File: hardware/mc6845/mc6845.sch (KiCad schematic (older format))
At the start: 20 parts, among them U1 MC6845, U10 AT28C16

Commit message: Add README, work on bitmap mode
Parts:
- J1: renamed from J?; footprint (none) -> Connector_PinHeader_2.54mm:PinHeader_2x20_P2.54mm_Vertical
- U10: footprint (none) -> Package_DIP:DIP-24_W10.16mm_Socket_LongPads
- U11, U13, U14, U15: renamed from U?; footprint (none) -> Package_DIP:DIP-14_W7.62mm_Socket_LongPads
- U12, U16, U17: renamed from U?; footprint (none) -> Package_DIP:DIP-16_W7.62mm_Socket_LongPads
- U2, U7: renamed from U?; footprint (none) -> Package_DIP:DIP-20_W7.62mm_Socket_LongPads
- X1: renamed from X?; footprint Oscillator:Oscillator_DIP-14 -> Package_DIP:DIP-4_W7.62mm_Socket_LongPads
- gave numbers to parts that had none: 1

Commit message: working on memory
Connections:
- net labels added: A[15..0], MA[15..0], PAGE[2..0]
- net labels removed: A[13..0], MA12, MA13, MA[13..0]
- wire segments 231 -> 229
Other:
- note added: "MA[15..12] to mux (RA, latch)"
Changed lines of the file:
@@
 F0 "memory" 50
 F1 "memory.sch" 50
-F2 "MA[13..0]" I L 6075 1300 50
-F3 "A[13..0]" I L 6075 1450 50
+F2 "MA[15..0]" I L 6075 1300 50
+F3 "A[15..0]" I L 6075 1450 50
 F4 "D[7..0]" B R 7075 1300 50
 F5 "LD[7..0]" O R 7075 1450 50
@@
 F10 "nBE" I L 6075 2225 50
 F11 "CCLK" I L 6075 2350 50
+F12 "MA[15..0]" I L 6075 2500 50
 $EndSheet
 Wire Bus Line
@@
 	7075 1300 7450 1300
 Text Label 5975 1300 2    50   ~ 0
-MA[13..0]
+MA[15..0]
 Wire Bus Line
 	7075 1450 7450 1450
@@
 D[7..0]
 Text Label 5675 1450 0    50   ~ 0
-A[13..0]
+A[15..0]
 Wire Wire Line
 	8000 2100 7650 2100
@@
 Wire Wire Line
 	4775 2475 5200 2475
-Text Label 5100 2275 2    50   ~ 0
-MA13
-Wire Wire Line
-	4775 2275 5200 2275
-Text Label 5100 2175 2    50   ~ 0
-MA12
-Wire Wire Line
-	4775 2175 5200 2175
 Text Label 5100 2075 2    50   ~ 0
 MA11
@@
 Wire Wire Line
 	8100 3875 8100 4325
+Wire Bus Line
+	6075 2500 5650 2500
+Text Label 5650 2500 0    50   ~ 0
+PAGE[2..0]
+Text Notes 5425 2975 0    75   ~ 0
+MA[15..12] to mux (RA, latch)
 $EndSCHEMATC

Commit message: working on 3D
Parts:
- removed A1: Arduino_UNO_R3, Module:Arduino_UNO_R3, symbol MCU_Module:Arduino_UNO_R3
- removed U2, U7: 74LS374, Package_DIP:DIP-20_W7.62mm_Socket_LongPads, symbol 74xx:74LS374
- removed X1: 25.175_DIP14, Package_DIP:DIP-4_W7.62mm_Socket_LongPads, symbol Oscillator:CXO_DIP14
- added X1: 25.175MHz, Package_DIP:DIP-8_W7.62mm_LongPads, symbol Oscillator:SG-8002DC
- U10: footprint Package_DIP:DIP-24_W10.16mm_Socket_LongPads -> Package_DIP:DIP-24_W15.24mm_LongPads
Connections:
- wire segments 229 -> 172
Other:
- note removed: "ADDRESS LATCH\n(Arduino)"

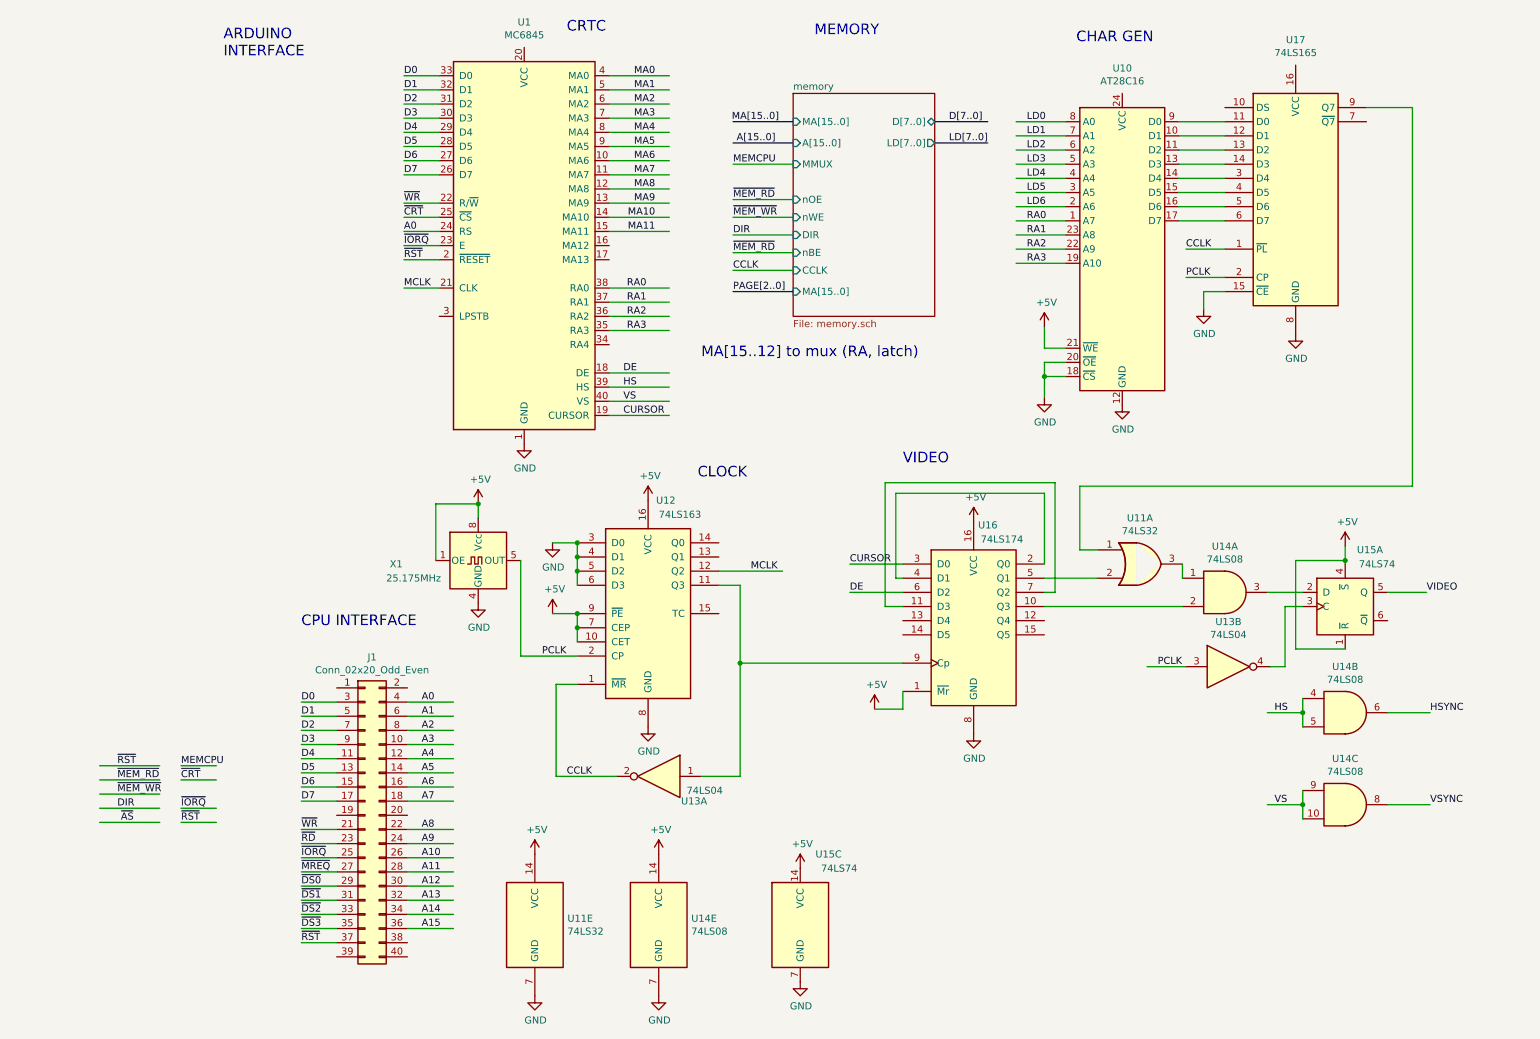
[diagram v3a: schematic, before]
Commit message: small tweaks, add Motorola AN851
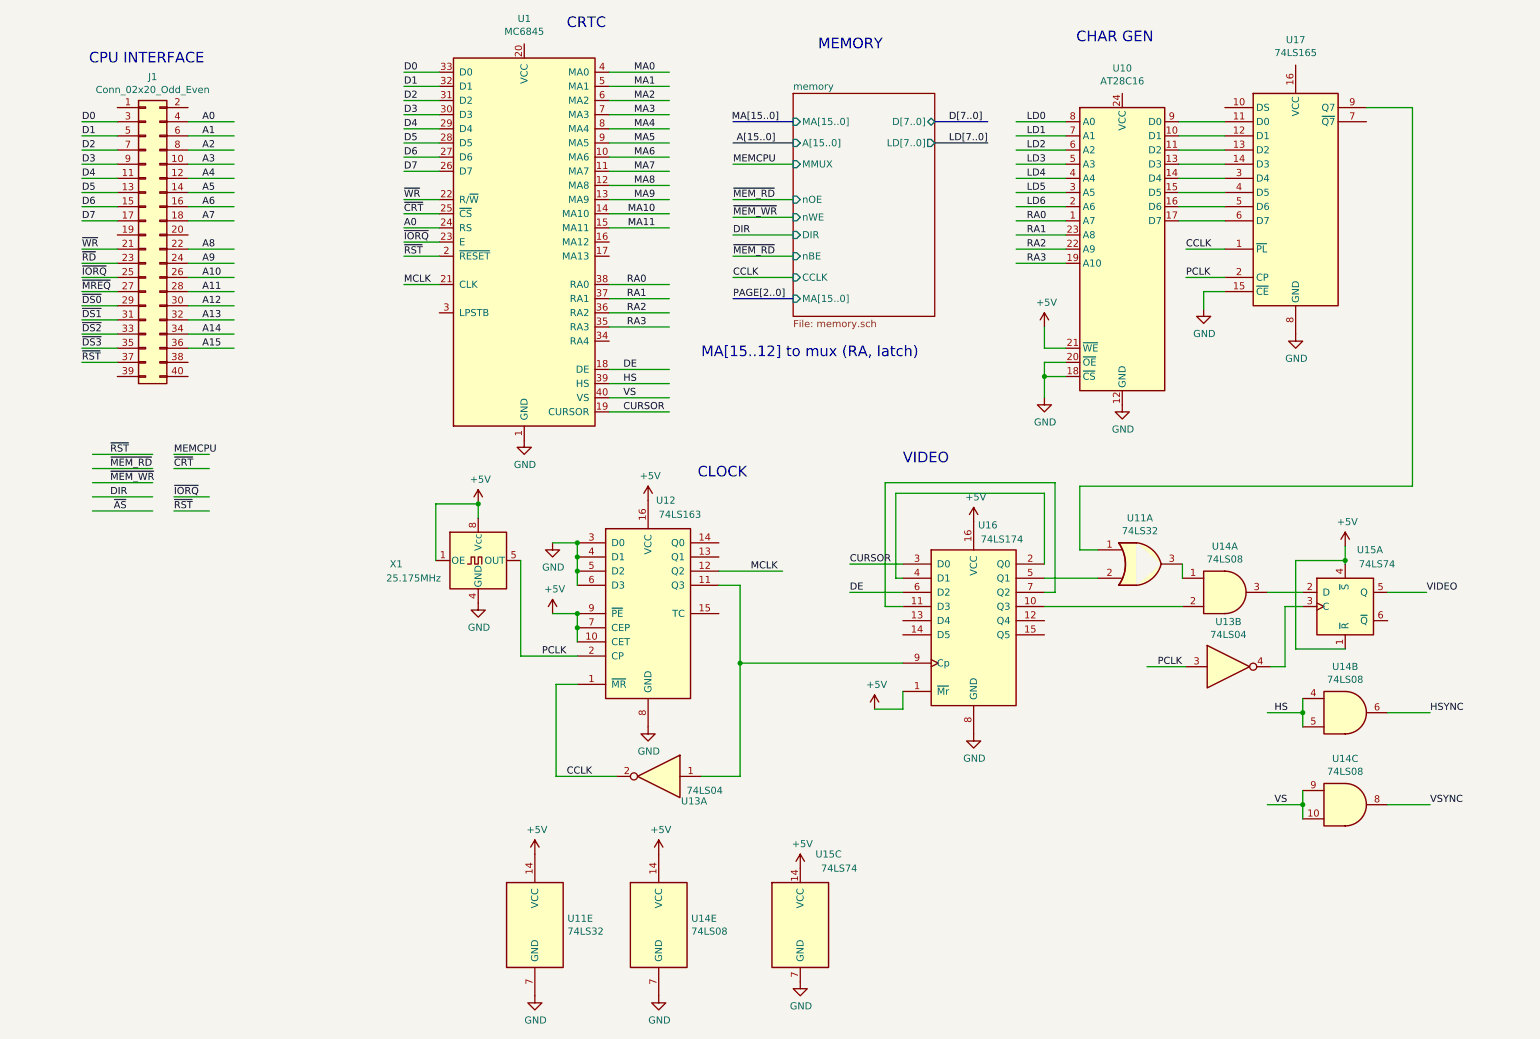
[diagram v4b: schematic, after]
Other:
- note removed: "ARDUINO\nINTERFACE"
- moved on the sheet: J1, U1

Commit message: memory wiring
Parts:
- added U?: 74LS157, symbol 74xx:74LS157
- added U?: 74LS374, symbol 74xx:74LS374
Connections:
- net labels added: MA12, MA13, MA14, MA15, PAGE0, PAGE1, PAGE2, PAGE[0..2]
- net labels removed: PAGE[2..0]
- wire segments 172 -> 201
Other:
- moved on the sheet: J1, U1

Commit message: working
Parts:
- removed U?: 74LS157, symbol 74xx:74LS157
- removed U?: 74LS374, symbol 74xx:74LS374
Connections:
- net labels added: A[11..0], MA[11..0], ~CRTC, ~VMEM
- net labels removed: A[15..0], MA12, MA13, MA14, MA15, MA[15..0], PAGE0, PAGE1, PAGE2, PAGE[0..2], ~DS0, ~DS1, ~DS2, ~DS3
- wire segments 201 -> 168
- no-connect marks 0 -> 4
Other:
- note removed: "MA[15..12] to mux (RA, latch)"
- moved on the sheet: U11A, U12, U13A, U13B, U14A, U14B, U14C, U15A, U16, U17, X1

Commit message: working on layout
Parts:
- removed U10: AT28C16, Package_DIP:DIP-24_W15.24mm_LongPads, symbol 28c256:AT28C16
- added C1, C10, C11, C12, C13, C14, C15, C16, C17, C2, C3, C4, C6, C7, C8, C9: 0.1uF, Capacitor_THT:C_Disc_D3.0mm_W1.6mm_P2.50mm, symbol Device:C_Small
- added C5: 10uF, Capacitor_THT:CP_Radial_Tantal_D5.5mm_P5.00mm, symbol Device:C_Small
- added H1, H2, H3, H4: MountingHole_Pad, MountingHole:MountingHole_2.7mm_M2.5_DIN965_Pad, symbol Mechanical:MountingHole_Pad
- added J2: DB15_Female_HighDensity, Connector_Dsub:DSUB-15-HD_Female_Horizontal_P2.29x2.54mm_EdgePinOffset9.40mm, symbol Connector:DB15_Female_HighDensity
- added J3: Conn_01x02, Connector_Molex:Molex_Mini-Fit_Jr_5566-02A_2x01_P4.20mm_Vertical, symbol Connector_Generic:Conn_01x02
- added unit 7 of U4
- added U8: 28C64A-15, Package_DIP:DIP-28_W15.24mm, symbol video_symbols:28C64
- J1: footprint Connector_PinHeader_2.54mm:PinHeader_2x20_P2.54mm_Vertical -> Connector_PinSocket_2.54mm:PinSocket_2x20_P2.54mm_Vertical
- U9: renamed from U17; value 74LS165 -> 74ALS165; CatNo (none) -> 296-33714-5-ND
- X1: value 25.175MHz -> MXO45HS-3C-25M1750; CatNo (none) -> 296-33714-5-ND; Supplier (none) -> Mouser
- renumbered U11 to U2, U12 to U3, U13 to U4, U14 to U5, U15 to U6, U16 to U7
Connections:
- net labels added: LD7
- net labels removed: DIR, MEMCPU, ~AS, ~MEM_RD, ~MEM_WR
- wire segments 168 -> 269
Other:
- note added: "25.175 MHz"
- note added: "8K configured as 4K"
- note added: "NOTE: LS too slow!"
- note added: "UPCO Graphics Systems\n80 x 30 monochrome video"
- moved on the sheet: U1, U2A, U2E, U3, U4A, U4B, U5A, U5B, U5C, U5E, U6A, U6C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

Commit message: started routing
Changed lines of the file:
@@
 U 1 1 5F3BC58A
 P 3500 2200
-F 0 "U1" H 3500 3778 50  0000 C CNN
-F 1 "MC6845" H 3500 3687 50  0000 C CNN
+F 0 "U1" H 3100 3600 50  0000 C CNN
+F 1 "MC6845" H 3800 3600 50  0000 C CNN
 F 2 "Package_DIP:DIP-40_W15.24mm" H 3550 850 50  0001 L CNN
 F 3 "http://pdf.datasheetcatalog.com/datasheet_pdf/motorola/MC6845L_and_MC6845P.pdf" H 3500 2200 50  0001 C CNN
@@
 	1    0    0    -1
 $EndComp
+$Comp
+L power:+5V #PWR0102
+U 1 1 6139CBDC
+P 3500 800
+F 0 "#PWR0102" H 3500 650 50  0001 C CNN
+F 1 "+5V" H 3515 973 50  0000 C CNN
+F 2 "" H 3500 800 50  0001 C CNN
+F 3 "" H 3500 800 50  0001 C CNN
+	1    3500 800
+	1    0    0    -1
+$EndComp
